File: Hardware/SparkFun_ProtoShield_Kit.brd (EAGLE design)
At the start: 64.8 x 53.3 mm, 27 parts

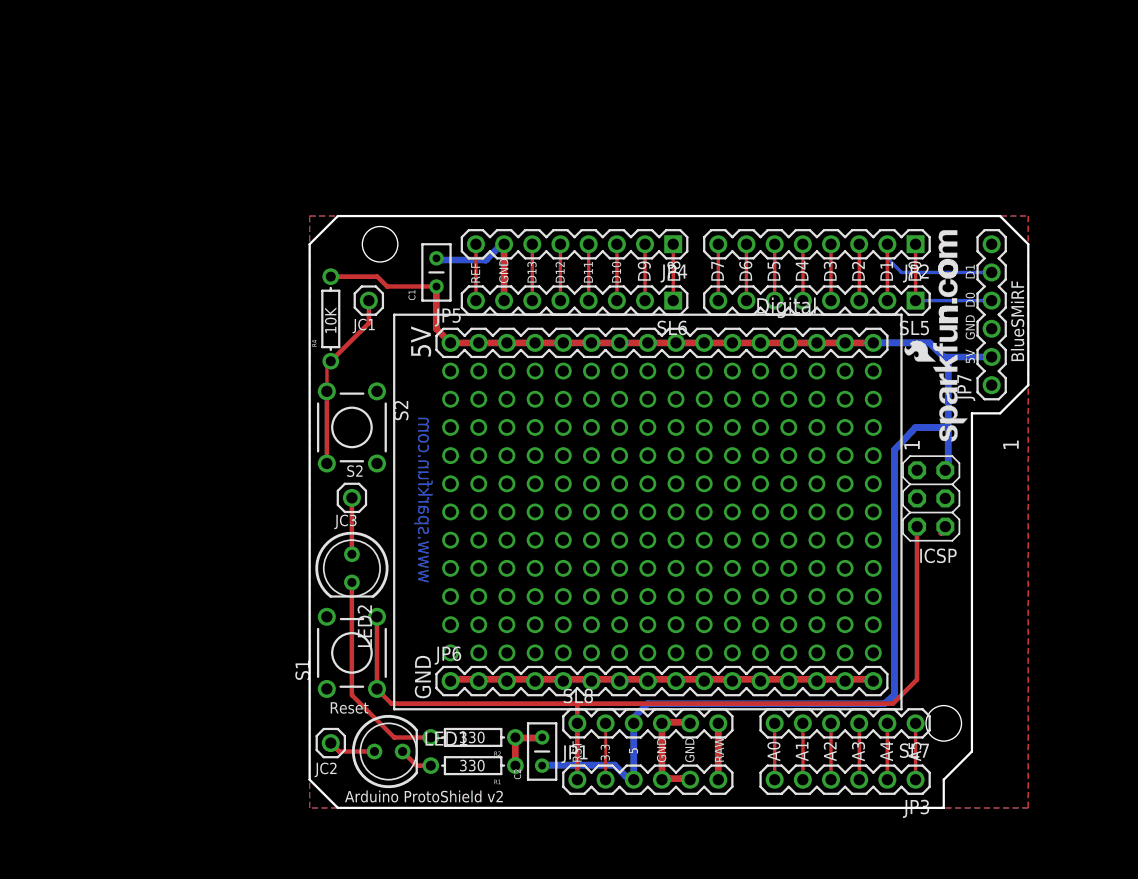
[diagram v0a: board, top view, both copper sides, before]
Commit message: WIP - basic hardware layout changes
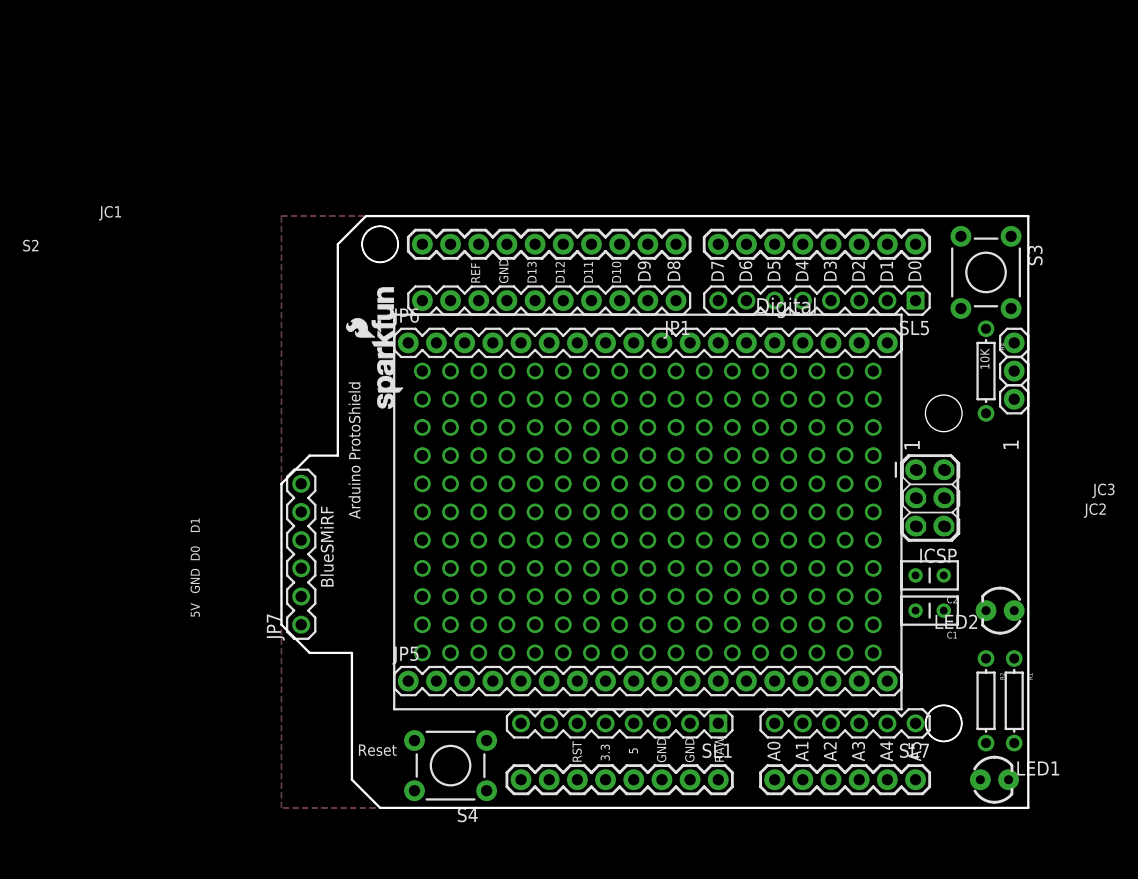
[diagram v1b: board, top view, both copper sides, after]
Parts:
- removed JP2: Digital1, SparkFun:1X08
- removed JP3: Analog, SparkFun:1X06
- removed JP4: Digital2, SparkFun:1X08
- removed S1: Reset, SparkFun:TACTILE-PTH
- removed S2: (no value), SparkFun:TACTILE-PTH
- removed SL6: (no value), SparkFun:1X08
- removed SL8: (no value), SparkFun:1X06
- added FRAME1: FRAME-LETTER, SparkFun-Aesthetics:CREATIVE_COMMONS
- added JP8: ARDUINO_R3_SHIELDR3_PROTO_SHIELD, TempLibrary:UNO_R3_PROTO_SHIELD
- added S3, S4: SWITCH-MOMENTARY-2PTH, SparkFun-Electromechanical:TACTILE-PTH
- added SL1: (no value), SparkFun:1X08
- JC1, JC2, JC3: value M01PTH -> (none); device SparkFun:1X01 -> SparkFun-Connectors:1X01
- JP1: value Power -> (none); device SparkFun:1X06 -> SparkFun-Connectors:1X10
- JP5, JP6: value M16PTH -> (none); device SparkFun:1X16 -> TempLibrary:1X18_ROUND
- LED1, LED2: device SparkFun:LED5MM -> SparkFun-LED:LED3MM
- U$1: value LOGO-SFENEW -> SFE_LOGO_NAME_FLAME.1_INCH; device SparkFun:SFE-NEW-WEBLOGO -> SparkFun-Aesthetics:SFE_LOGO_NAME_FLAME_.1
- U$2: value CREATIVE_COMMONS -> REVISION; device SparkFun:CREATIVE_COMMONS -> SparkFun-Aesthetics:REVISION
- moved JC2 70.1 mm to (63.5, 39.4), turned to 0 degrees
- moved JP7 65.9 mm to (-0.76, 16.5)
- moved JC3 61.3 mm to (63.5, 41.9)
- moved R4 59.2 mm to (61.0, 39.4), turned to 270 degrees
- moved JC1 58.8 mm to (63.5, 36.8)
- moved LED2 58.5 mm to (62.2, 17.8), turned to 180 degrees
- moved LED1 54.7 mm to (61.7, 2.54)
- moved C1 54.3 mm to (57.1, 17.8), turned to 180 degrees
- moved U$1 50.9 mm to (8.51, 35.6)
- moved R1 49.1 mm to (63.5, 9.65), turned to 270 degrees
- moved R2 46.3 mm to (61.0, 9.65), turned to 270 degrees
- moved JP1 44.1 mm to (33.0, 45.7), turned to 180 degrees
- moved C2 40.1 mm to (57.1, 21.0), turned to 180 degrees
- moved JP5 30.7 mm to (8.89, 11.4)
- moved JP6 30.7 mm to (8.89, 41.9)
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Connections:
- removed net 3.3V: JP1.2, SL8.2
- removed net VIN: JP1.6, SL8.6
- new net N$1: JP8.IOREF, SL1.7
- new net N$183: JP8.GND@2, SL1.3
- new net N$184: SL1.2
- new net N$185: JP8.VIN, SL1.1
- new net N$186: JP1.9, JP8.SDA
- new net N$187: JP1.10, JP8.SCL
- new net N$2: JP8.RES, SL1.6
- new net N$8: JP8.3.3V, SL1.5
- new net N$9: JP8.5V, SL1.4
- net 5V: no longer JP1.3, SL8.3
- net A0: now also JP8.A0; no longer JP3.6
- net A1: now also JP8.A1; no longer JP3.5
- net A2: now also JP8.A2; no longer JP3.4
- net A3: now also JP8.A3; no longer JP3.3
- net A4: now also JP8.A4; no longer JP3.2
- net A5: now also JP8.A5; no longer JP3.1
- net AREF: now also JP1.8; no longer JP4.8, SL6.8
- net D10: now also JP1.3, JP8.D10; no longer JP4.3, SL6.3
- net D11: now also JP1.4, JP8.D11; no longer JP4.4, SL6.4
- net D12: now also JP1.5, JP8.D12; no longer JP4.5, SL6.5
- net D13: now also JP1.6, JP8.D13; no longer JP4.6, SL6.6
- net D2: now also JP8.D2; no longer JP2.3
- net D3: now also JP8.D3; no longer JP2.4
- net D4: now also JP8.D4; no longer JP2.5
- net D5: now also JP8.D5; no longer JP2.6
- net D6: now also JP8.D6; no longer JP2.7
- net D7: now also JP8.D7; no longer JP2.8
- net D8: now also JP1.1, JP8.D8; no longer JP4.1, SL6.1
- net D9: now also JP1.2, JP8.D9; no longer JP4.2, SL6.2
- net GND: now also JP1.7, S3.1, S4.1; no longer JP1.4, JP1.5, JP4.7, S1.1, S1.2, S2.1, S2.2, SL6.7, SL8.4, SL8.5
- net RES: now also S3.3; no longer S2.3, S2.4
- net RESET: now also S4.3; no longer JP1.1, S1.3, S1.4, SL8.1
- net RX: now also JP8.RX; no longer JP2.1
- net TX: now also JP8.TX; no longer JP2.2
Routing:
- net 5V: track 141.7 -> 0.00 mm
- net RESET: track 77.4 -> 0.00 mm
- net GND: track 66.2 -> 0.66 mm
- net N$7: track 18.9 -> 0.00 mm
- net TX: track 16.3 -> 0.00 mm
- net RES: track 16.2 -> 0.00 mm
- net RX: track 11.9 -> 0.00 mm
- net LED2: track 5.08 -> 0.00 mm
- net VIN: track 5.08 -> 0.00 mm
- net A5: track 5.08 -> 0.00 mm
- net A4: track 5.08 -> 0.00 mm
- net A3: track 5.08 -> 0.00 mm
- net A2: track 5.08 -> 0.00 mm
- net A1: track 5.08 -> 0.00 mm
- net A0: track 5.08 -> 0.00 mm
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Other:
- board size 64.8 x 53.3 mm -> 67.3 x 53.3 mm
- board text added: "Arduino ProtoShield"
- board text removed: "Arduino ProtoShield v2"
- board text removed: "www.sparkfun.com"

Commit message: Ready for engineering review
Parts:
- added LOGO1: OSHW-LOGOS, SparkFun-Aesthetics:OSHW-LOGO-S
- added SJ1, SJ2, SJ3, SJ4: JUMPER-PAD-2-NC_BY_TRACE, SparkFun-Passives:PAD-JUMPER-2-NC_BY_TRACE_YES_SILK
- JP5, JP6: device TempLibrary:1X18_ROUND -> SparkFun-Connectors:1X19
- U$1: value SFE_LOGO_NAME_FLAME.1_INCH -> SFE_LOGO_NAME.1_INCH; device SparkFun-Aesthetics:SFE_LOGO_NAME_FLAME_.1 -> SparkFun-Aesthetics:SFE_LOGO_NAME_.1
- moved JC3 62.1 mm to (16.5, 1.27), turned to 180 degrees
- moved LED2 61.6 mm to (2.54, 2.54), turned to 270 degrees
- moved JC2 58.5 mm to (19.1, 1.27), turned to 270 degrees
- moved JC1 55.0 mm to (21.6, 1.27), turned to 270 degrees
- moved JP8 54.6 mm to (53.3, 64.8), turned to 180 degrees
- moved R2 52.1 mm to (9.53, 1.27), turned to 180 degrees
- moved JP7 52.0 mm to (16.5, 65.5), turned to 0 degrees
- moved R4 50.4 mm to (27.9, 1.27), turned to 0 degrees
- moved S4 49.0 mm to (4.45, 52.1), turned to 90 degrees
- moved BB1 48.3 mm to (8.89, 57.1), turned to 270 degrees
- moved JP5 47.1 mm to (11.4, 58.4), turned to 270 degrees
- moved SL7 47.1 mm to (7.62, 10.2), turned to 90 degrees
- moved S3 46.2 mm to (48.3, 3.81), turned to 0 degrees
- moved C2 43.5 mm to (15.7, 7.62)
- moved C1 39.4 mm to (19.1, 7.62), turned to 0 degrees
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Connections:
- net N$186 renamed SDA
- net N$187 renamed SCL
- removed net N$183: JP8.GND@2, SL1.3
- removed net N$184: SL1.2
- new net N$219: JP7.3, SJ3.1
- new net N$220: JP7.2, SJ4.1
- new net NC3: SL1.8
- net 5V: now also JP5.17, JP5.18, JP5.19, JP8.5V, SJ4.2, SL1.4; no longer JP7.2
- net AREF: now also JP8.AREF
- net GND: now also JP6.17, JP6.18, JP6.19, JP8.GND@0, JP8.GND@1, JP8.GND@2, SJ3.2, SL1.2, SL1.3; no longer JP7.3
- net N$2: now also JP7.5, SJ1.1; no longer JP8.RES, SL1.6
- net N$9: now also JP7.4, SJ2.1; no longer JP8.5V, SL1.4
- net RESET: now also JP8.RES, SL1.6
- net RX: now also SJ2.2; no longer JP7.4
- net TX: now also SJ1.2; no longer JP7.5
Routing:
- net 5V: track 0.00 -> 96.9 mm
- net RX: track 0.00 -> 76.7 mm
- net TX: track 0.00 -> 75.2 mm
- net RESET: track 0.00 -> 63.1 mm
- net LED1: track 0.00 -> 23.9 mm
- net LED2: track 0.00 -> 15.4 mm
- net RES: track 0.00 -> 5.74 mm
- net N$8: track 0.00 -> 5.08 mm
- net N$185: track 0.00 -> 5.08 mm
- net N$1: track 0.00 -> 5.08 mm
- net A5: track 0.00 -> 5.08 mm
- net A4: track 0.00 -> 5.08 mm
- net A3: track 0.00 -> 5.08 mm
- net A2: track 0.00 -> 5.08 mm
- net A1: track 0.00 -> 5.08 mm
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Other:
- board size 67.3 x 53.3 mm -> 53.3 x 67.3 mm
- board text added: "IOR"
- board text added: "LED1"
- board text added: "LED2"
- board text added: "NC"
- board text added: "Nathan Seidle"
- board text added: "SCL"
- board text added: "SDA"
- board text added: "SW2"
- board text added: "Toni Klopfenstein"
- board text added: "Units: Inches"
- board text added: "v30"
- board text removed: "5"
- board text removed: "S2"

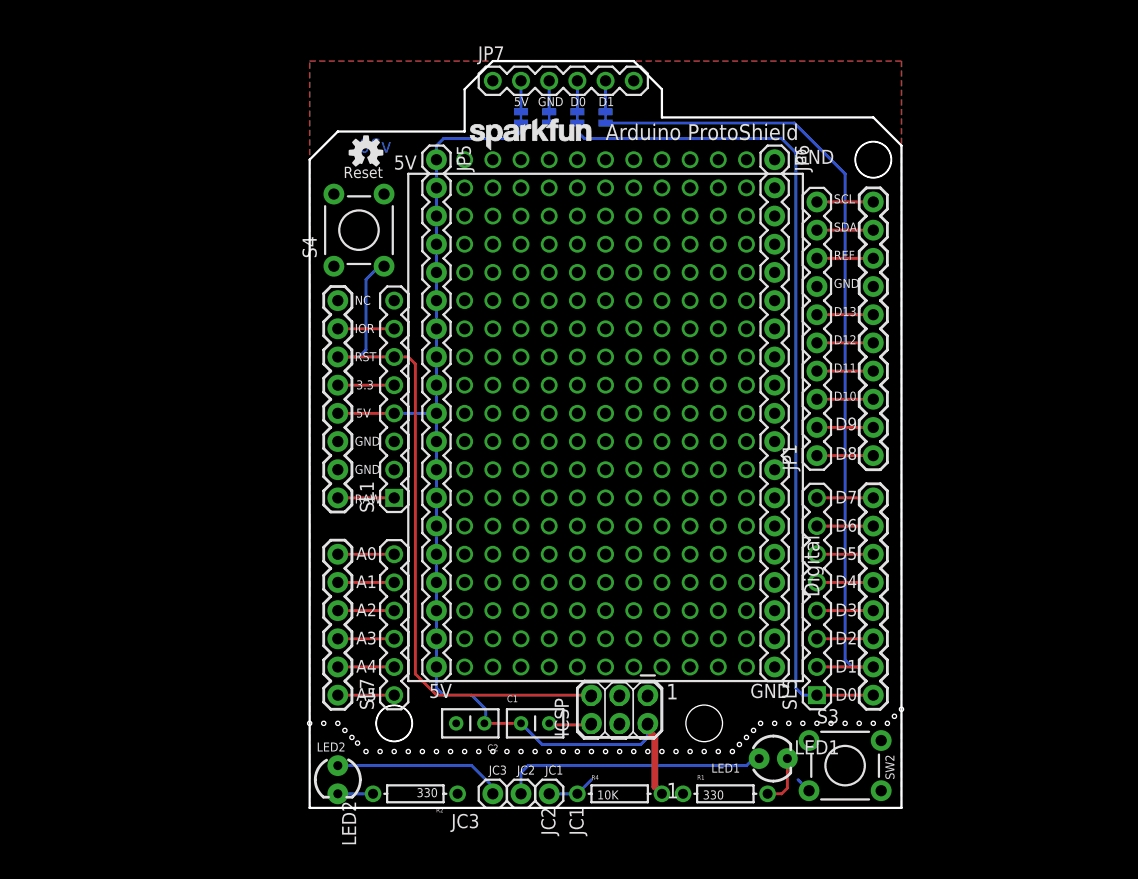
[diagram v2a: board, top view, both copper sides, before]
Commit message: Fixing part names, adding additional connector from engineering review
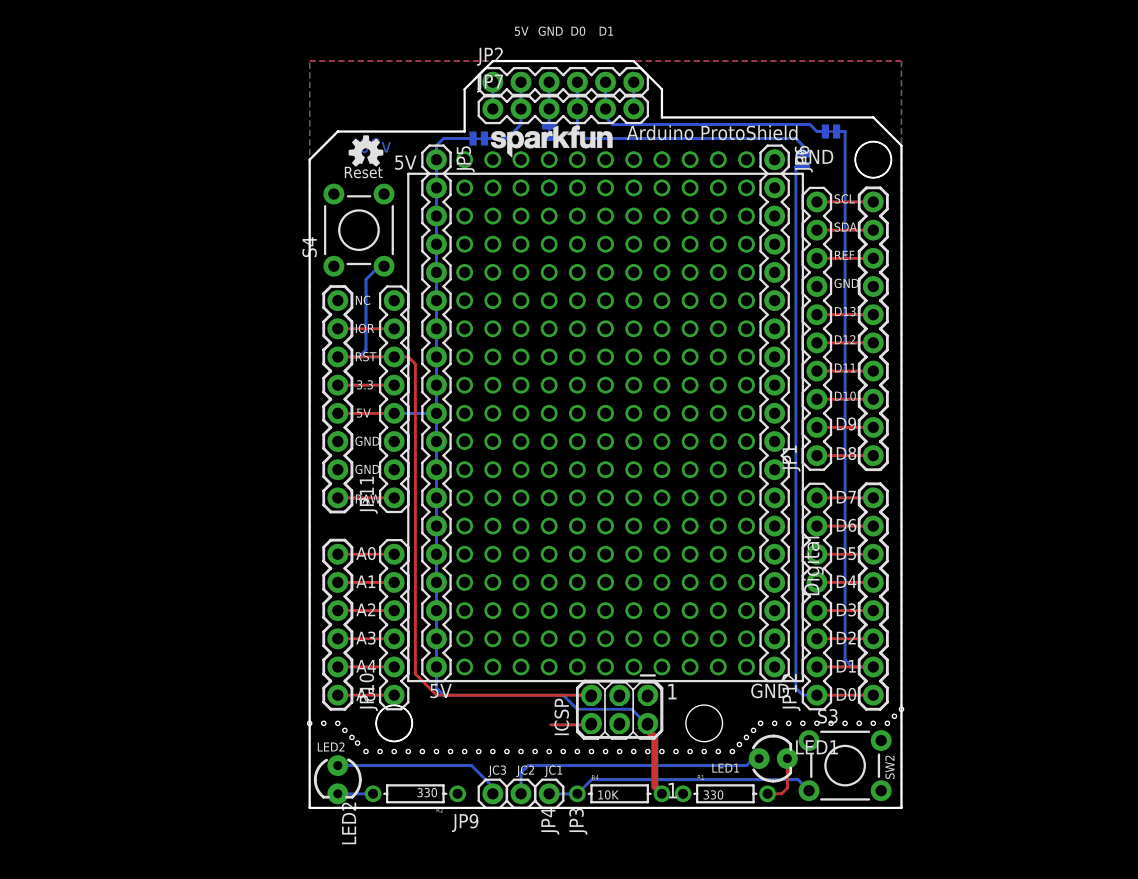
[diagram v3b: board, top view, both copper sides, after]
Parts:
- removed C1, C2: 0.1uF, SparkFun:CAP-PTH-SMALL2
- removed SL1, SL5: (no value), SparkFun:1X08
- removed SL7: (no value), SparkFun:1X06
- added JP10, JP2: (no value), SparkFun-Connectors:1X06
- added JP11, JP12: (no value), SparkFun-Connectors:1X08_ROUND
- JP7: device SparkFun:1X06 -> SparkFun-Connectors:1X06
- moved SJ2 20.7 mm to (44.5, 58.4)
- moved SJ1 20.4 mm to (47.0, 61.0), turned to 180 degrees
- moved SJ4 4.26 mm to (15.2, 60.3), turned to 0 degrees
- moved JP7 2.54 mm to (16.5, 63.0)
- moved U$1 2.01 mm to (15.9, 58.2)
- moved SJ3 1.27 mm to (21.6, 61.0)
- renumbered JC1 to JP3, JC2 to JP4, JC3 to JP9
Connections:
- removed net N$2: JP7.5, SJ1.1
- removed net N$219: JP7.3, SJ3.1
- removed net N$220: JP7.2, SJ4.1
- removed net N$9: JP7.4, SJ2.1
- new net FTDI_5V: JP2.2, JP7.2, SJ4.1
- new net FTDI_GND: JP2.3, JP7.3, SJ3.1
- new net FTDI_RX: JP2.4, JP7.4, SJ2.1
- new net FTDI_TX: JP2.5, JP7.5, SJ1.1
- net 5V: now also JP11.4; no longer C1.1, C2.1, SL1.4
- net A0: now also JP10.6; no longer SL7.6
- net A1: now also JP10.5; no longer SL7.5
- net A2: now also JP10.4; no longer SL7.4
- net A3: now also JP10.3; no longer SL7.3
- net A4: now also JP10.2; no longer SL7.2
- net A5: now also JP10.1; no longer SL7.1
- net D2: now also JP12.3; no longer SL5.3
- net D3: now also JP12.4; no longer SL5.4
- net D4: now also JP12.5; no longer SL5.5
- net D5: now also JP12.6; no longer SL5.6
- net D6: now also JP12.7; no longer SL5.7
- net D7: now also JP12.8; no longer SL5.8
- net GND: now also JP11.2, JP11.3; no longer C1.2, C2.2, SL1.2, SL1.3
- net N$1: now also JP11.7; no longer SL1.7
- net N$185: now also JP11.1; no longer SL1.1
- net N$8: now also JP11.5; no longer SL1.5
- net NC1: now also JP2.1
- net NC2: now also JP2.6
- net NC3: now also JP11.8; no longer SL1.8
- net RESET: now also JP11.6; no longer SL1.6
- net RX: now also JP12.1; no longer SL5.1
- net TX: now also JP12.2; no longer SL5.2
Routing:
- net FTDI_RX: track 0.00 -> 26.1 mm
- net FTDI_TX: track 0.00 -> 23.5 mm
- net RX: track 76.7 -> 55.0 mm
- net TX: track 75.2 -> 56.3 mm
- net RES: track 5.74 -> 24.4 mm
- net 5V: track 96.9 -> 88.5 mm
- net FTDI_5V: track 0.00 -> 7.64 mm
- net FTDI_GND: track 0.00 -> 3.94 mm
- net N$9: track 2.79 -> 0.00 mm
- net N$220: track 2.79 -> 0.00 mm
- net N$219: track 2.79 -> 0.00 mm
- net N$2: track 2.79 -> 0.00 mm
- net NC2: track 0.00 -> 2.41 mm
- net NC1: track 0.00 -> 2.41 mm

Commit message: Updates from engineering review
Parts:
- moved SJ1 13.3 mm to (33.7, 61.0)
- moved SJ2 10.8 mm to (33.7, 58.4), turned to 180 degrees
- moved SJ3 2.54 mm to (21.6, 58.4), turned to 180 degrees
- moved SJ4 2.29 mm to (14.0, 58.4)
- moved U$1 2.01 mm to (15.2, 56.3)
- moved JP7 1.90 mm to (16.5, 61.1)
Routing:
- net FTDI_RX: track 26.1 -> 14.5 mm
- net TX: track 56.3 -> 66.6 mm
- net FTDI_TX: track 23.5 -> 13.2 mm
- net RX: track 55.0 -> 63.7 mm
- net FTDI_5V: track 7.64 -> 11.2 mm
- net FTDI_GND: track 3.94 -> 7.30 mm
- net 5V: track 88.5 -> 85.7 mm
- net NC2: track 2.41 -> 4.32 mm
- net NC1: track 2.41 -> 4.32 mm
- net GND: track 3.62 -> 3.11 mm, vias 0 -> 1
- removed copper zone on layer 16, net GND

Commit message: WIP-bumping annular rings
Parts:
- moved LED2 0.64 mm to (2.54, 1.91), turned to 0 degrees
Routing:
- net LED2: track 15.4 -> 16.8 mm
- net N$7: track 3.17 -> 2.01 mm
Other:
- outline, holes or cut-outs redrawn

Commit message: Updates from checklist
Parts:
- BB1: device SparkFun:BREADBOARD-MINI -> SparkFun-Boards:BREADBOARD-MINI
- ICSP: device pinhead:2X03 -> SparkFun-Connectors:2X3
- R1, R2, R4: device SparkFun:AXIAL-0.3 -> SparkFun-Resistors:AXIAL-0.3
- moved ICSP 3.68 mm to (30.4, 11.4)
- moved JP8 1.27 mm to (53.3, 66.0)
- moved BB1 1.27 mm to (8.89, 58.4)
- moved JP1 1.27 mm to (45.7, 33.0)
- moved LOGO1 1.27 mm to (5.08, 60.3)
- moved S4 1.27 mm to (4.45, 53.3)
- moved FRAME1 1.27 mm to (1.80, -14.6)
- moved JP10 1.27 mm to (7.62, 11.4)
- moved JP11 1.27 mm to (7.62, 29.2)
- moved JP12 1.27 mm to (45.7, 11.4)
- moved U$2 1.27 mm to (13.3, -17.1)
- moved JP2 1.27 mm to (16.5, 66.7)
- moved JP5 1.27 mm to (11.4, 59.7)
- moved JP6 1.27 mm to (41.9, 59.7)
- moved JP7 1.27 mm to (16.5, 62.4)
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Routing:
- net GND: track 3.11 -> 24.7 mm, vias 1 -> 3
- net LED2: track 16.8 -> 18.7 mm
- net 5V: track 85.7 -> 86.9 mm
- net RES: track 24.4 -> 25.5 mm, vias 0 -> 1
- net N$7: track 2.01 -> 2.80 mm
- added copper zone on layer 16, net GND
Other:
- board size 53.3 x 67.3 mm -> 53.3 x 68.6 mm
- board text added: "RX"
- board text added: "TX"
